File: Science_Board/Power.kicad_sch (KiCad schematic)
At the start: 51 parts, among them IC1 TCKE603RA, IC2 TCKE603RA, IC3 TCKE603RM, J21 Molex_Megafit_02, J22 Molex_Megafit_02, J3 Molex_Megafit_02, J4 Molex_Megafit_02, Q1 BS250, Q2 NMOS, Q3 NMOS, Q4 NMOS, U1 AP63205WU

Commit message: finished footprints
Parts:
- D1, D10, D7, D8, D9: footprint Package_DIP:DIP-40_W15.24mm -> Diode_SMD:D_SOD-323_HandSoldering
- D2, D3, D4: footprint Diode_SMD:D_0603_1608Metric_Pad1.05x0.95mm_HandSolder -> LED_SMD:LED_0603_1608Metric_Pad1.05x0.95mm_HandSolder
- D5, D6: footprint Package_DIP:DIP-40_W15.24mm -> Diode_SMD:D_SOD-123
- Q2, Q3, Q4: footprint Package_DFN_QFN:Nordic_AQFN-94-1EP_7x7mm_P0.4mm -> Package_TO_SOT_SMD:SOT-23-3
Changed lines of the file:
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@@
 			)
 		)
-		(property "Footprint" "Package_DIP:DIP-40_W15.24mm"
+		(property "Footprint" "Diode_SMD:D_SOD-323_HandSoldering"
 			(at 62.23 38.1 0)
 			(hide yes)
@@
 			)
 		)
-		(property "Footprint" "Package_DIP:DIP-40_W15.24mm"
+		(property "Footprint" "Diode_SMD:D_SOD-323_HandSoldering"
 			(at 27.94 81.28 0)
 			(hide yes)
@@
 			)
 		)
-		(property "Footprint" "Package_DIP:DIP-40_W15.24mm"
+		(property "Footprint" "Diode_SMD:D_SOD-123"
 			(at 213.36 88.9 0)
 			(hide yes)
@@
 			)
 		)
-		(property "Footprint" "Diode_SMD:D_0603_1608Metric_Pad1.05x0.95mm_HandSolder"
+		(property "Footprint" "LED_SMD:LED_0603_1608Metric_Pad1.05x0.95mm_HandSolder"
 			(at 35.56 121.92 0)
 			(hide yes)
@@
 			)
 		)
-		(property "Footprint" "Diode_SMD:D_0603_1608Metric_Pad1.05x0.95mm_HandSolder"
+		(property "Footprint" "LED_SMD:LED_0603_1608Metric_Pad1.05x0.95mm_HandSolder"
 			(at 53.34 121.92 0)
 			(hide yes)
@@
 			)
 		)
-		(property "Footprint" "Package_DIP:DIP-40_W15.24mm"
+		(property "Footprint" "Diode_SMD:D_SOD-323_HandSoldering"
 			(at 118.11 63.5 0)
 			(hide yes)
@@
 			)
 		)
-		(property "Footprint" "Package_DIP:DIP-40_W15.24mm"
+		(property "Footprint" "Diode_SMD:D_SOD-323_HandSoldering"
 			(at 214.63 138.43 0)
 			(hide yes)
@@
 			)
 		)
-		(property "Footprint" "Package_DIP:DIP-40_W15.24mm"
+		(property "Footprint" "Diode_SMD:D_SOD-323_HandSoldering"
 			(at 27.94 39.37 0)
 			(hide yes)
@@
 			)
 		)
-		(property "Footprint" "Package_DFN_QFN:Nordic_AQFN-94-1EP_7x7mm_P0.4mm"
+		(property "Footprint" "Package_TO_SOT_SMD:SOT-23-3"
 			(at 40.64 33.02 0)
 			(hide yes)
@@
 			)
 		)
-		(property "Footprint" "Diode_SMD:D_0603_1608Metric_Pad1.05x0.95mm_HandSolder"
+		(property "Footprint" "LED_SMD:LED_0603_1608Metric_Pad1.05x0.95mm_HandSolder"
 			(at 16.51 121.92 0)
 			(hide yes)
@@
 			)
 		)
-		(property "Footprint" "Package_DFN_QFN:Nordic_AQFN-94-1EP_7x7mm_P0.4mm"
+		(property "Footprint" "Package_TO_SOT_SMD:SOT-23-3"
 			(at 40.64 74.93 0)
 			(hide yes)
@@
 			)
 		)
-		(property "Footprint" "Package_DIP:DIP-40_W15.24mm"
+		(property "Footprint" "Diode_SMD:D_SOD-123"
 			(at 35.56 170.18 0)
 			(hide yes)
@@
 			)
 		)
-		(property "Footprint" "Package_DFN_QFN:Nordic_AQFN-94-1EP_7x7mm_P0.4mm"
+		(property "Footprint" "Package_TO_SOT_SMD:SOT-23-3"
 			(at 74.93 31.75 0)
 			(hide yes)

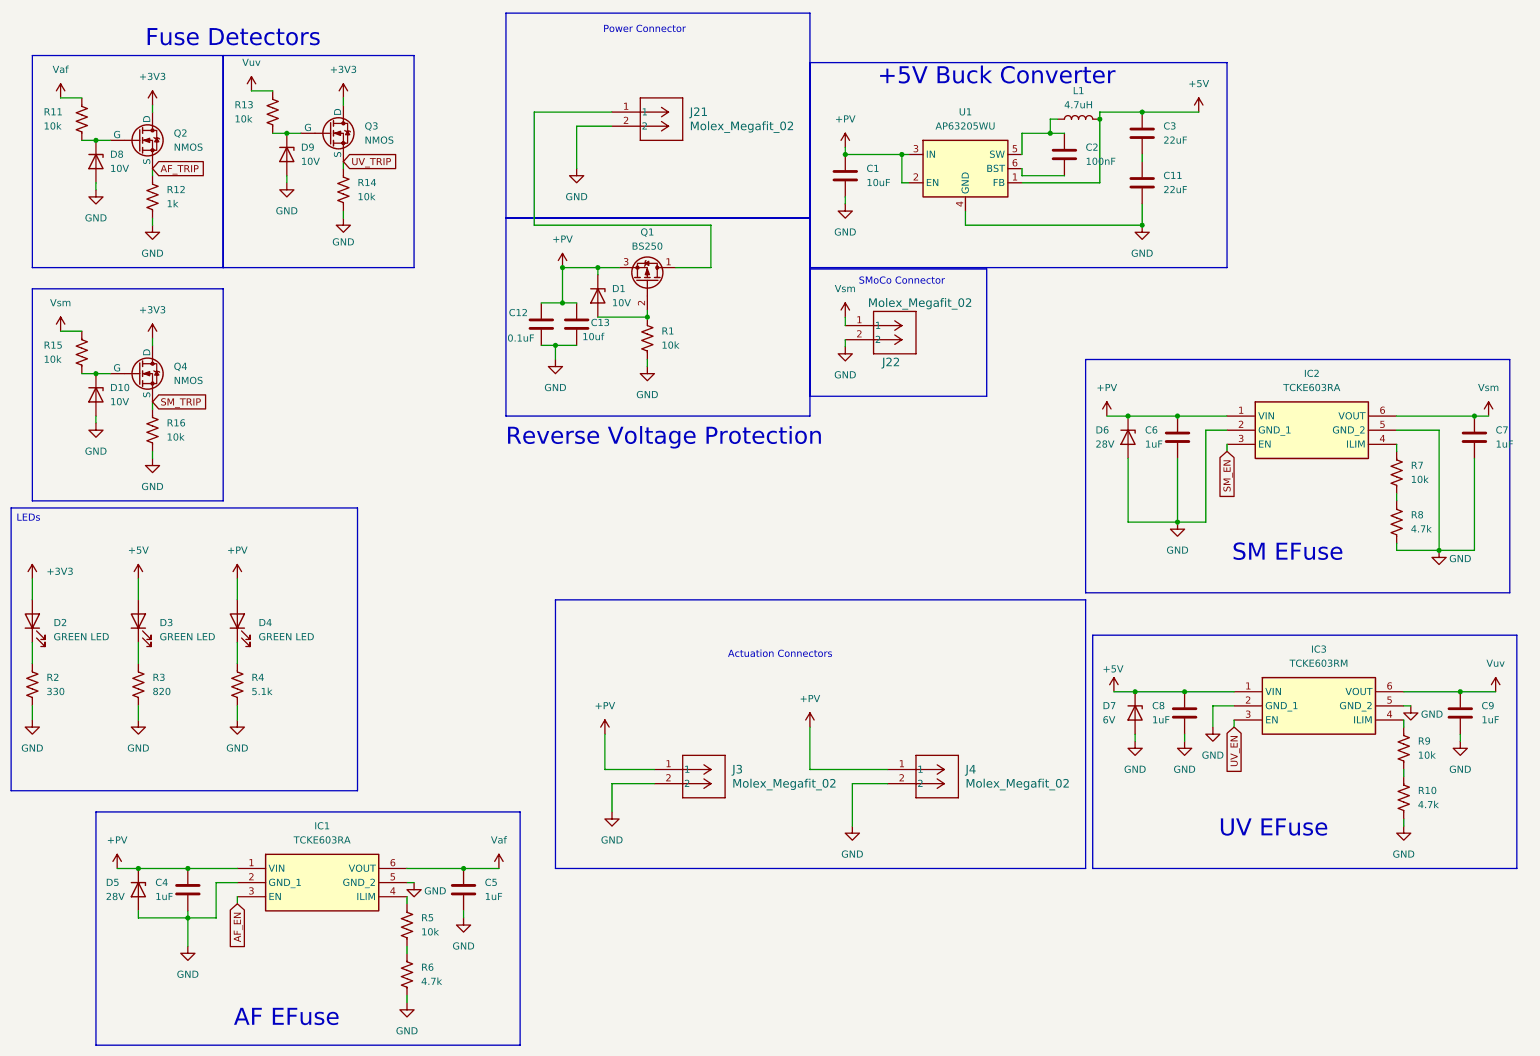
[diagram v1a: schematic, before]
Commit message: created button sheet added LEDs for the buttons and the E-fuses
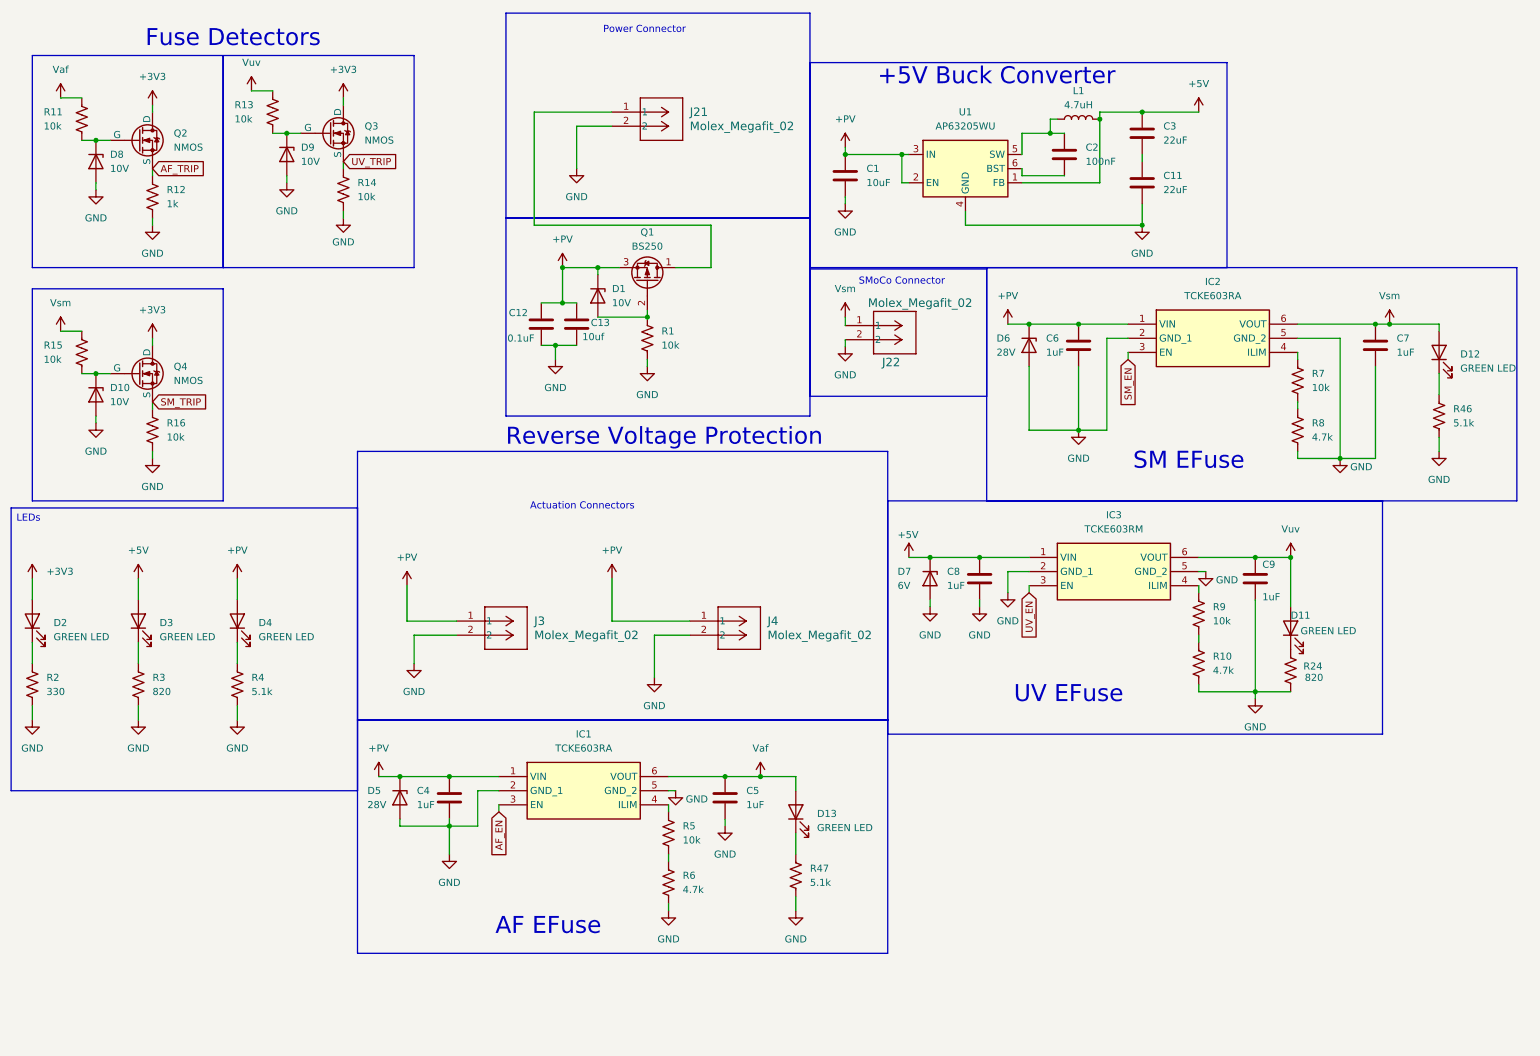
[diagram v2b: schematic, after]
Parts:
- added D11, D12, D13: GREEN LED, LED_SMD:LED_0603_1608Metric_Pad1.05x0.95mm_HandSolder, symbol Device:LED
- added R24: 820, Resistor_SMD:R_0603_1608Metric_Pad0.98x0.95mm_HandSolder, symbol Device:R_US
- added R46, R47: 5.1k, Resistor_SMD:R_0603_1608Metric_Pad0.98x0.95mm_HandSolder, symbol Device:R_US
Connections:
- net GND: now also R24.2, R46.2, R47.2
- net Vaf: now also D13.2 (A)
- net Vsm: now also D12.2 (A)
- net Vuv: now also D11.2 (A)
- new net: D13.1 (K), R47.1
- new net: D11.1 (K), R24.1
- new net: D12.1 (K), R46.1
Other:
- moved on the sheet: C4, C5, C6, C7, C8, C9, D5, D6, D7, IC1, IC2, IC3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

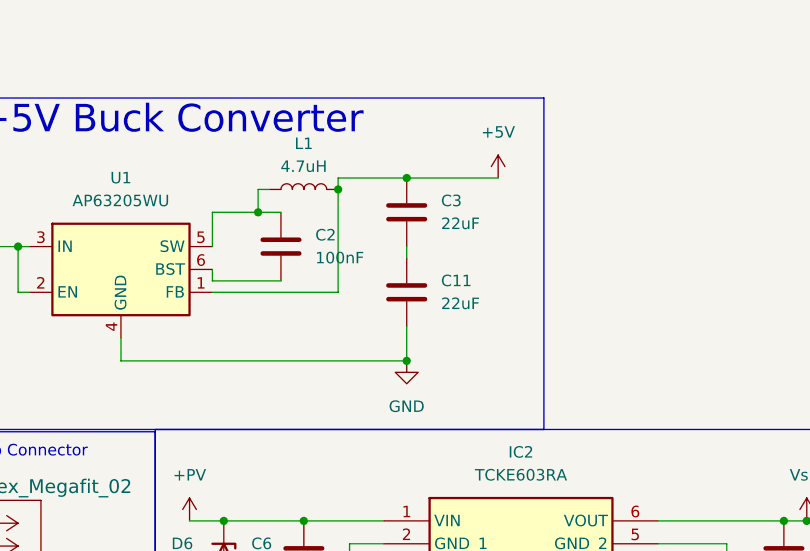
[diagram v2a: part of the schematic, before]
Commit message: changed capacitor and started on layout
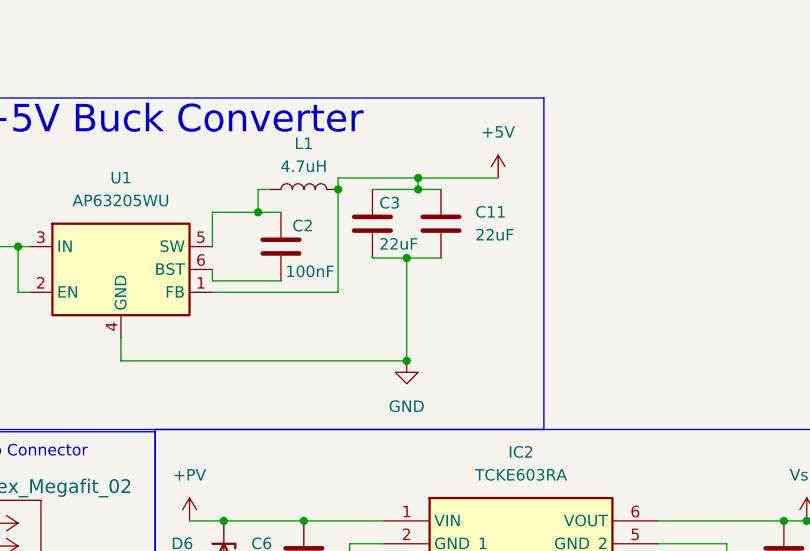
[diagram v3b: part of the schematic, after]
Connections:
- net +5V: now also C11.1
- net GND: now also C3.2
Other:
- moved on the sheet: C3
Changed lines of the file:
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@@
 	)
 	(junction
+		(at 215.9 39.37)
+		(diameter 0)
+		(color 0 0 0 0)
+	)
+	(junction
 		(at 82.55 149.86)
 		(diameter 0)
@@
 	)
 	(junction
+		(at 217.17 30.48)
+		(diameter 0)
+		(color 0 0 0 0)
+	)
+	(junction
 		(at 118.11 58.42)
 		(diameter 0)
@@
 	)
 	(junction
-		(at 215.9 30.48)
+		(at 217.17 31.75)
 		(diameter 0)
 		(color 0 0 0 0)
@@
 	(wire
 		(pts
+			(xy 219.71 39.37) (xy 215.9 39.37)
+		)
+		(stroke
+			(width 0)
+			(type default)
+		)
+	)
+	(wire
+		(pts
 			(xy 209.55 71.12) (xy 209.55 87.63)
 		)
@@
 	(wire
 		(pts
+			(xy 217.17 31.75) (xy 212.09 31.75)
+		)
+		(stroke
+			(width 0)
+			(type default)
+		)
+	)
+	(wire
+		(pts
 			(xy 100.33 154.94) (xy 100.33 156.21)
 		)
@@
 	(wire
 		(pts
-			(xy 215.9 46.99) (xy 215.9 50.8)
+			(xy 215.9 39.37) (xy 215.9 50.8)
 		)
 		(stroke
@@
 	(wire
 		(pts
-			(xy 215.9 30.48) (xy 208.28 30.48)
+			(xy 208.28 30.48) (xy 217.17 30.48)
 		)
 		(stroke
@@
 	(wire
 		(pts
+			(xy 217.17 31.75) (xy 219.71 31.75)
+		)
+		(stroke
+			(width 0)
+			(type default)
+		)
+	)
+	(wire
+		(pts
 			(xy 82.55 157.48) (xy 82.55 158.75)
 		)
@@
 	(wire
 		(pts
-			(xy 215.9 30.48) (xy 226.06 30.48)
-		)
-		(stroke
-			(width 0)
-			(type default)
-		)
-	)
-	(wire
-		(pts
 			(xy 130.81 163.83) (xy 130.81 165.1)
 		)
@@
 	(wire
 		(pts
-			(xy 215.9 38.1) (xy 215.9 39.37)
+			(xy 212.09 39.37) (xy 215.9 39.37)
 		)
 		(stroke
@@
 	(wire
 		(pts
+			(xy 217.17 30.48) (xy 217.17 31.75)
+		)
+		(stroke
+			(width 0)
+			(type default)
+		)
+	)
+	(wire
+		(pts
 			(xy 78.74 149.86) (xy 82.55 149.86)
 		)
@@
 		)
 	)
+	(wire
+		(pts
+			(xy 217.17 30.48) (xy 226.06 30.48)
+		)
+		(stroke
+			(width 0)
+			(type default)
+		)
+	)
 	(global_label "UV_EN"
 		(shape input)
@@
 	)
 	(symbol
-		(lib_id "Device:C")
-		(at 215.9 43.18 0)
+		(lib_id "power:GND")
+		(at 132.08 152.4 0)
 		(unit 1)
 		(body_style 1)
@@
 		(in_pos_files yes)
 		(dnp no)
-		(fields_autoplaced yes)
-		(property "Reference" "C11"
-			(at 219.71 41.9099 0)
+		(property "Reference" "#PWR018"
+			(at 132.08 158.75 0)
+			(hide yes)
 			(show_name no)
 			(do_not_autoplace no)
@@
 					(size 1.27 1.27)
 				)
-				(justify left)
 			)
 		)
-		(property "Value" "22uF"
-			(at 219.71 44.4499 0)
+		(property "Value" "GND"
+			(at 135.89 153.924 0)
 			(show_name no)
 			(do_not_autoplace no)
@@
 					(size 1.27 1.27)
 				)
-				(justify left)
 			)
 		)
-		(property "Footprint" "Capacitor_SMD:C_0603_1608Metric_Pad1.08x0.95mm_HandSolder"
-			(at 216.8652 46.99 0)
+		(property "Footprint" ""
+			(at 132.08 152.4 0)
 			(hide yes)
 			(show_name no)
@@
 		)
 		(property "Datasheet" ""
-			(at 215.9 43.18 0)
+			(at 132.08 152.4 0)
 			(hide yes)
 			(show_name no)
@@
 			)
 		)
-		(property "Description" "Unpolarized capacitor"
-			(at 215.9 43.18 0)
+		(property "Description" "Power symbol creates a global label with name \"GND\" , ground"
+			(at 132.08 152.4 0)
 			(hide yes)
 			(show_name no)
@@
 		(pin "1"
 		)
-		(pin "2"
-		)
 		(instances
 			(project "Science_Board"
 				(path "/4f5c5f7f-4385-4de2-96ca-2ae741ebf691/6219bf49-5574-4710-86f4-9f93da84ad76"
-					(reference "C11")
+					(reference "#PWR018")
 					(unit 1)
 				)
@@
 	(symbol
 		(lib_id "power:GND")
-		(at 132.08 152.4 0)
+		(at 186.69 119.38 0)
 		(unit 1)
 		(body_style 1)
@@
 		(in_pos_files yes)
 		(dnp no)
-		(property "Reference" "#PWR018"
-			(at 132.08 158.75 0)
+		(fields_autoplaced yes)
+		(property "Reference" "#PWR036"
+			(at 186.69 125.73 0)
 			(hide yes)
 			(show_name no)
@@
 		)
 		(property "Value" "GND"
-			(at 135.89 153.924 0)
+			(at 186.69 124.46 0)
 			(show_name no)
 			(do_not_autoplace no)
@@
 		)
 		(property "Footprint" ""
-			(at 132.08 152.4 0)
+			(at 186.69 119.38 0)
 			(hide yes)
 			(show_name no)
@@
 		)
 		(property "Datasheet" ""
-			(at 132.08 152.4 0)
+			(at 186.69 119.38 0)
 			(hide yes)
 			(show_name no)
@@
 		)
 		(property "Description" "Power symbol creates a global label with name \"GND\" , ground"
-			(at 132.08 152.4 0)
+			(at 186.69 119.38 0)
 			(hide yes)
 			(show_name no)
@@
 			(project "Science_Board"
 				(path "/4f5c5f7f-4385-4de2-96ca-2ae741ebf691/6219bf49-5574-4710-86f4-9f93da84ad76"
-					(reference "#PWR018")
+					(reference "#PWR036")
 					(unit 1)
 				)
@@
 	(symbol
 		(lib_id "power:GND")
-		(at 186.69 119.38 0)
+		(at 251.46 92.71 0)
 		(unit 1)
 		(body_style 1)
@@
 		(in_pos_files yes)
 		(dnp no)
-		(fields_autoplaced yes)
-		(property "Reference" "#PWR036"
-			(at 186.69 125.73 0)
+		(property "Reference" "#PWR031"
+			(at 251.46 99.06 0)
 			(hide yes)
 			(show_name no)
@@
 		)
 		(property "Value" "GND"
-			(at 186.69 124.46 0)
+			(at 255.27 94.234 0)
 			(show_name no)
 			(do_not_autoplace no)
@@
 		)
 		(property "Footprint" ""
-			(at 186.69 119.38 0)
+			(at 251.46 92.71 0)
 			(hide yes)
 			(show_name no)
@@
 		)
 		(property "Datasheet" ""
-			(at 186.69 119.38 0)
+			(at 251.46 92.71 0)
 			(hide yes)
 			(show_name no)
@@
 		)
 		(property "Description" "Power symbol creates a global label with name \"GND\" , ground"
-			(at 186.69 119.38 0)
+			(at 251.46 92.71 0)
 			(hide yes)
 			(show_name no)
@@
 			(project "Science_Board"
 				(path "/4f5c5f7f-4385-4de2-96ca-2ae741ebf691/6219bf49-5574-4710-86f4-9f93da84ad76"
-					(reference "#PWR036")
+					(reference "#PWR031")
 					(unit 1)
 				)
@@
 	)
 	(symbol
-		(lib_id "power:GND")
-		(at 251.46 92.71 0)
+		(lib_id "Device:C")
+		(at 219.71 35.56 0)
 		(unit 1)
 		(body_style 1)
@@
 		(in_pos_files yes)
 		(dnp no)
-		(property "Reference" "#PWR031"
-			(at 251.46 99.06 0)
-			(hide yes)
+		(fields_autoplaced yes)
+		(property "Reference" "C11"
+			(at 223.52 34.2899 0)
 			(show_name no)
 			(do_not_autoplace no)
@@
 					(size 1.27 1.27)
 				)
+				(justify left)
 			)
 		)
-		(property "Value" "GND"
-			(at 255.27 94.234 0)
+		(property "Value" "22uF"
+			(at 223.52 36.8299 0)
 			(show_name no)
 			(do_not_autoplace no)
@@
 					(size 1.27 1.27)
 				)
+				(justify left)
 			)
 		)
-		(property "Footprint" ""
-			(at 251.46 92.71 0)
+		(property "Footprint" "Capacitor_SMD:C_0603_1608Metric_Pad1.08x0.95mm_HandSolder"
+			(at 220.6752 39.37 0)
 			(hide yes)
 			(show_name no)
@@
 		)
 		(property "Datasheet" ""
-			(at 251.46 92.71 0)
+			(at 219.71 35.56 0)
 			(hide yes)
 			(show_name no)
@@
 			)
 		)
-		(property "Description" "Power symbol creates a global label with name \"GND\" , ground"
-			(at 251.46 92.71 0)
+		(property "Description" "Unpolarized capacitor"
+			(at 219.71 35.56 0)
 			(hide yes)
 			(show_name no)
@@
 		(pin "1"
 		)
+		(pin "2"
+		)
 		(instances
 			(project "Science_Board"
 				(path "/4f5c5f7f-4385-4de2-96ca-2ae741ebf691/6219bf49-5574-4710-86f4-9f93da84ad76"
-					(reference "#PWR031")
+					(reference "C11")
 					(unit 1)
 				)
@@
 	(symbol
 		(lib_id "Device:C")
-		(at 215.9 34.29 0)
+		(at 212.09 35.56 0)
 		(unit 1)
 		(body_style 1)
@@
 		(in_pos_files yes)
 		(dnp no)
-		(fields_autoplaced yes)
 		(property "Reference" "C3"
-			(at 219.71 33.0199 0)
+			(at 212.852 33.274 0)
 			(show_name no)
 			(do_not_autoplace no)
@@
 		)
 		(property "Value" "22uF"
-			(at 219.71 35.5599 0)
+			(at 212.852 37.846 0)
 			(show_name no)
 			(do_not_autoplace no)
@@
 		)
 		(property "Footprint" "Capacitor_SMD:C_0603_1608Metric_Pad1.08x0.95mm_HandSolder"
-			(at 216.8652 38.1 0)
+			(at 213.0552 39.37 0)
 			(hide yes)
 			(show_name no)
@@
 		)
 		(property "Datasheet" ""
-			(at 215.9 34.29 0)
+			(at 212.09 35.56 0)
 			(hide yes)
 			(show_name no)
@@
 		)
 		(property "Description" "Unpolarized capacitor"
-			(at 215.9 34.29 0)
+			(at 212.09 35.56 0)
 			(hide yes)
 			(show_name no)
@@
 		(in_pos_files yes)
 		(dnp no)
-		(fields_autoplaced yes)
 		(property "Reference" "C2"
-			(at 205.74 36.8299 0)
+			(at 203.2 35.814 0)
 			(show_name no)
 			(do_not_autoplace no)
@@
 		)
 		(property "Value" "100nF"
-			(at 205.74 39.3699 0)
+			(at 202.438 40.894 0)
 			(show_name no)
 			(do_not_autoplace no)
